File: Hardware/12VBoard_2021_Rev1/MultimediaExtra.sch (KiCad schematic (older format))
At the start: 33 parts, among them Q1 CSD18537NQ5A, Q2 CSD18531Q5A, Q9 IRLML2060, U5 LT1910, U7 LM5116, U8 INA198

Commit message: Started work on updated layout
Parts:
- removed C11: 2.2uF, Capacitor_SMD:C_0603_1608Metric_Pad1.05x0.95mm_HandSolder, symbol Device:C_Small
- removed C12: 100uF, Capacitor_SMD:C_0603_1608Metric_Pad1.05x0.95mm_HandSolder, symbol Device:C_Small
- removed C13: 1uF, Capacitor_SMD:C_0603_1608Metric_Pad1.05x0.95mm_HandSolder, symbol Device:C_Small
- removed C14: 100nF, Capacitor_SMD:C_0603_1608Metric_Pad1.05x0.95mm_HandSolder, symbol Device:C_Small
- removed C15: 100uF, Capacitor_THT:CP_Radial_D6.3mm_P2.50mm, symbol Device:CP1_Small
- removed C16: 10pF, Capacitor_SMD:C_0603_1608Metric_Pad1.05x0.95mm_HandSolder, symbol Device:CP1_Small
- removed C17: 120pF, Capacitor_SMD:C_0603_1608Metric_Pad1.05x0.95mm_HandSolder, symbol Device:CP1_Small
- removed C19: 470pF, Capacitor_SMD:C_0603_1608Metric_Pad1.05x0.95mm_HandSolder, symbol Device:C_Small
- removed C20: 33pF, Capacitor_SMD:C_0603_1608Metric_Pad1.05x0.95mm_HandSolder, symbol Device:C_Small
- removed D12: 1.25V 250mA, Diode_SMD:D_SOD-323_HandSoldering, symbol Device:D_Small
- removed L6: 10uH, Inductor_THT:L_Radial_D27.9mm_P20.07mm_Vishay_IHB-3, symbol Device:L_Small
- removed Q1: CSD18537NQ5A, Package_SON:VSONP-8-1EP_5x6_P1.27mm, symbol 12VBoard_2021_Rev1-rescue:CSD18537NQ5A
- removed Q2: CSD18531Q5A, Package_SON:VSONP-8-1EP_5x6_P1.27mm, symbol 12VBoard_2021_Rev1-rescue:CSD18531Q5A
- removed R10: 2.26K, Resistor_SMD:R_0603_1608Metric_Pad1.05x0.95mm_HandSolder, symbol Device:R_Small
- removed R11: 86.6K, Resistor_SMD:R_0603_1608Metric_Pad1.05x0.95mm_HandSolder, symbol Device:R_Small
- removed R12: 9.76k, Resistor_SMD:R_0603_1608Metric_Pad1.05x0.95mm_HandSolder, symbol Device:R_Small
- removed R13: 261K, Resistor_SMD:R_0603_1608Metric_Pad1.05x0.95mm_HandSolder, symbol Device:R_Small
- removed R8: 5m, Resistor_SMD:R_0603_1608Metric_Pad1.05x0.95mm_HandSolder, symbol Device:R_Small
- removed R9: 36.5K, Resistor_SMD:R_0603_1608Metric_Pad1.05x0.95mm_HandSolder, symbol Device:R_Small
- removed U7: LM5116, Package_SO:TSSOP-20_4.4x6.5mm_P0.65mm, symbol 12VBoard_2021_Rev1-rescue:LM5116
- added C17: 0.1uF, Capacitor_SMD:C_0603_1608Metric_Pad1.05x0.95mm_HandSolder, symbol Device:C_Small
- added D16: Aux Mount Acuation Gree, Diode_SMD:D_0603_1608Metric_Pad1.05x0.95mm_HandSolder, symbol Device:LED
- added R19: 5.1K, Resistor_SMD:R_0603_1608Metric_Pad1.05x0.95mm_HandSolder, symbol Device:R
- added R20: 0.01, Resistor_SMD:R_0603_1608Metric_Pad1.05x0.95mm_HandSolder, symbol Device:R
- added R23: 1.2k, Resistor_SMD:R_0603_1608Metric_Pad1.05x0.95mm_HandSolder, symbol Device:R
- added U19: LT1910, Package_SO:SOIC-8-N7_3.9x4.9mm_P1.27mm, symbol MRDT_ICs:LT1910
- added U20: FDS66900AS, Package_SO:SOIC-8_3.9x4.9mm_P1.27mm, symbol 12VBoard_2021_Rev1:FDS66900AS
- C18: value 100uF -> 10uF; footprint Capacitor_THT:CP_Radial_D6.3mm_P2.50mm -> Capacitor_THT:CP_Radial_D5.0mm_P2.00mm
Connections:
- net labels added: 12Actuation, 12V5AMultimedia, 12V5AON
- net labels removed: 12V10AMultiMedia, MULT_COMPFB, MULT_CS, MULT_CSGDEMB, MULT_HB, MULT_HO, MULT_LO, MULT_SW, MULT_VCC, MULT_VOUTVCCX, PackVoltage
- wire segments 163 -> 83
- no-connect marks 1 -> 0
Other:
- moved on the sheet: D14, R18

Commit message: Layout for high current
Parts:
- U20: symbol 12VBoard_2021_Rev1:FDS66900AS -> 12VBoard_2021_Rev1-rescue:FDS66900AS-12VBoard_2021_Rev1
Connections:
- net labels added: 12V5AMultiMedia
- net labels removed: 12V5AMultimedia
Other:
- moved on the sheet: C17, C18, D14, F1, R14, R18, R19, R20, TP5, U19, U8

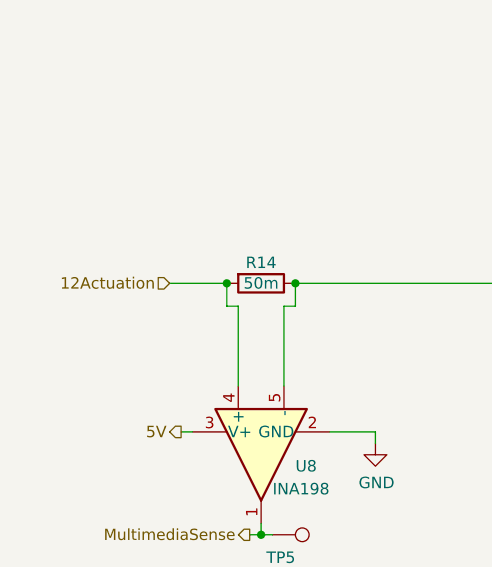
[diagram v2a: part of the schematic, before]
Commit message: fisnished board traces
still a problem with 12VAcuation
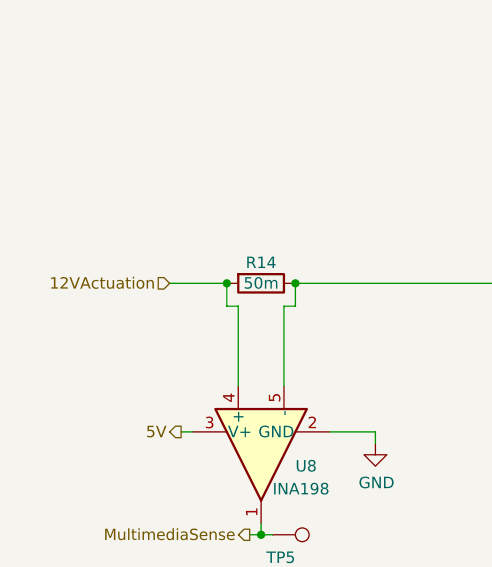
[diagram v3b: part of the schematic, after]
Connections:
- net 12Actuation renamed 12VActuation
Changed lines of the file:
@@
 	5475 1250 5525 1250
 Text HLabel 1300 5500 0    50   Input ~ 0
-12Actuation
+12VActuation
 Text HLabel 6925 5100 2    50   Input ~ 0
 12V5AMultiMedia

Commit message: Started work on BOM
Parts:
- F1: value 10A -> 5A
- R14: footprint Package_TO_SOT_THT:TO-126-2_Vertical -> Resistor_SMD:R_2010_5025Metric_Pad1.52x2.65mm_HandSolder
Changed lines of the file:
@@
 EESchema Schematic File Version 4
-LIBS:12VBoard_2021_Rev1-cache
 EELAYER 30 0
 EELAYER END
@@
 F 0 "R14" V 1610 5500 50  0000 C CNN
 F 1 "50m" V 1700 5500 50  0000 C CNN
-F 2 "Package_TO_SOT_THT:TO-126-2_Vertical" V 1630 5500 50  0001 C CNN
+F 2 "Resistor_SMD:R_2010_5025Metric_Pad1.52x2.65mm_HandSolder" V 1630 5500 50  0001 C CNN
 F 3 "~" H 1700 5500 50  0001 C CNN
 	1    1700 5500
@@
 AR Path="/5F74F36B/5F8236F9/5F92ED48" Ref="F1"  Part="1"
 F 0 "F1" V 2820 5500 50  0000 C CNN
-F 1 "10A" V 2900 5500 50  0000 C CNN
+F 1 "5A" V 2900 5500 50  0000 C CNN
 F 2 "MRDT_Passives:ATC_Fuse_Block" V 2830 5500 50  0001 C CNN
 F 3 "~" H 2900 5500 50  0001 C CNN

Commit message: Discovered problems, will fix on next pushes
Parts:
- R14: value 50m -> 20m
- R20: footprint Resistor_SMD:R_0603_1608Metric_Pad1.05x0.95mm_HandSolder -> Resistor_SMD:R_0805_2012Metric_Pad1.15x1.40mm_HandSolder
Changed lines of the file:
@@
 P 1700 5500
 F 0 "R14" V 1610 5500 50  0000 C CNN
-F 1 "50m" V 1700 5500 50  0000 C CNN
+F 1 "20m" V 1700 5500 50  0000 C CNN
 F 2 "Resistor_SMD:R_2010_5025Metric_Pad1.52x2.65mm_HandSolder" V 1630 5500 50  0001 C CNN
 F 3 "~" H 1700 5500 50  0001 C CNN
@@
 F 0 "R20" H 5670 4305 50  0000 L CNN
 F 1 "0.01" V 5625 4225 50  0000 L CNN
-F 2 "Resistor_SMD:R_0603_1608Metric_Pad1.05x0.95mm_HandSolder" V 5555 4300 50  0001 C CNN
+F 2 "Resistor_SMD:R_0805_2012Metric_Pad1.15x1.40mm_HandSolder" V 5555 4300 50  0001 C CNN
 F 3 "~" H 5625 4300 50  0001 C CNN
 	1    5625 4300

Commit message: Fixed problem
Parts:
- D14: value Multimedia Actuation Green -> LED
- D16: value Aux Mount Acuation Gree -> LED
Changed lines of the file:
@@
 $Descr A4 11693 8268
 encoding utf-8
-Sheet 6 8
+Sheet 8 8
 Title ""
 Date ""
@@
 AR Path="/5F74F36B/5F8236F9/5F955B40" Ref="D14"  Part="1"
 F 0 "D14" V 6939 5583 50  0000 R CNN
-F 1 "Multimedia Actuation Green" V 6848 5583 50  0000 R CNN
+F 1 "LED" V 6848 5583 50  0000 R CNN
 F 2 "Diode_SMD:D_0603_1608Metric_Pad1.05x0.95mm_HandSolder" H 6900 5700 50  0001 C CNN
 F 3 "~" H 6900 5700 50  0001 C CNN
@@
 AR Path="/5F74F36B/5F8236F9/5FD64214" Ref="D16"  Part="1"
 F 0 "D16" V 7539 2333 50  0000 R CNN
-F 1 "Aux Mount Acuation Gree" V 7448 2333 50  0000 R CNN
+F 1 "LED" V 7448 2333 50  0000 R CNN
 F 2 "Diode_SMD:D_0603_1608Metric_Pad1.05x0.95mm_HandSolder" H 7500 2450 50  0001 C CNN
 F 3 "~" H 7500 2450 50  0001 C CNN

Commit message: Started Rev 2
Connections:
- net 12V5AMultiMedia: now also U20.1 (Source), U20.2 (Source), U20.3 (Source); no longer U20.5 (Drain), U20.6 (Drain), U20.7 (Drain), U20.8 (Drain)
- new net: R20.2, U19.6 (SENSE), U20.5 (Drain), U20.6 (Drain), U20.7 (Drain), U20.8 (Drain)
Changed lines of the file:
@@
 MultimediaCTL_Act
-$Comp
-L MRDT_ICs:LT1910 U?
-U 1 1 5FD04938
-P 4425 4775
-AR Path="/5F74F36B/5F971CD6/5FD04938" Ref="U?"  Part="1"
-AR Path="/5F74F36B/5F8236F9/5FD04938" Ref="U19"  Part="1"
-F 0 "U19" H 4800 5462 60  0000 C CNN
-F 1 "LT1910" H 4800 5356 60  0000 C CNN
-F 2 "Package_SO:SOIC-8-N7_3.9x4.9mm_P1.27mm" H 4425 4775 60  0001 C CNN
-F 3 "" H 4425 4775 60  0001 C CNN
-	1    4425 4775
-	1    0    0    -1
-$EndComp
 $Comp
 L Device:C_Small C?
@@
 F 3 "" H 6425 4975 50  0001 C CNN
 	1    6375 4825
-	1    0    0    -1
-$EndComp
-Wire Wire Line
-	5375 4675 5925 4675
-Wire Wire Line
-	5625 4525 5625 4775
+	-1   0    0    1
+$EndComp
 Wire Wire Line
 	5625 4975 5925 4975
@@
 	6900 4675 6900 4775
 Wire Wire Line
-	6825 4975 6900 4975
-Connection ~ 6900 4975
-Wire Wire Line
-	6900 4975 6900 5100
-Wire Wire Line
 	6825 4875 6900 4875
 Connection ~ 6900 4875
-Wire Wire Line
-	6900 4875 6900 4975
 Wire Wire Line
 	6825 4775 6900 4775
@@
 Wire Wire Line
 	3050 5500 3250 5500
+Wire Wire Line
+	6900 4875 6900 5100
+Wire Wire Line
+	5625 4525 5625 4675
+Wire Wire Line
+	5625 4675 5925 4675
+Connection ~ 5625 4675
+Wire Wire Line
+	5625 4675 5625 4775
+Wire Wire Line
+	5540 4675 5540 4595
+Wire Wire Line
+	5540 4595 5905 4595
+Wire Wire Line
+	5905 4595 5905 4535
+Wire Wire Line
+	5905 4535 6945 4535
+Wire Wire Line
+	6945 4535 6945 4975
+Wire Wire Line
+	6945 4975 6825 4975
+$Comp
+L MRDT_ICs:LT1910 U?
+U 1 1 5FD04938
+P 4425 4775
+AR Path="/5F74F36B/5F971CD6/5FD04938" Ref="U?"  Part="1"
+AR Path="/5F74F36B/5F8236F9/5FD04938" Ref="U19"  Part="1"
+F 0 "U19" H 4800 5462 60  0000 C CNN
+F 1 "LT1910" H 4800 5356 60  0000 C CNN
+F 2 "Package_SO:SOIC-8-N7_3.9x4.9mm_P1.27mm" H 4425 4775 60  0001 C CNN
+F 3 "" H 4425 4775 60  0001 C CNN
+	1    4425 4775
+	1    0    0    -1
+$EndComp
+Wire Wire Line
+	5540 4675 5375 4675
 $EndSCHEMATC
